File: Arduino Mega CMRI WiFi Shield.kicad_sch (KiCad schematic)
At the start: 22 parts, among them J10 61300411121, J11 61300411121, J12 61300411121, J13 61300411121, J14 61300411121, J15 61300411121, J16 61300411121, J17 61300411121, J18 61300311121, J2 61300411121, J3 61300411121, J4 61300411121, J5 61300411121, J6 61300411121, J7 61300411121, J8 61300411121, J9 61300411121

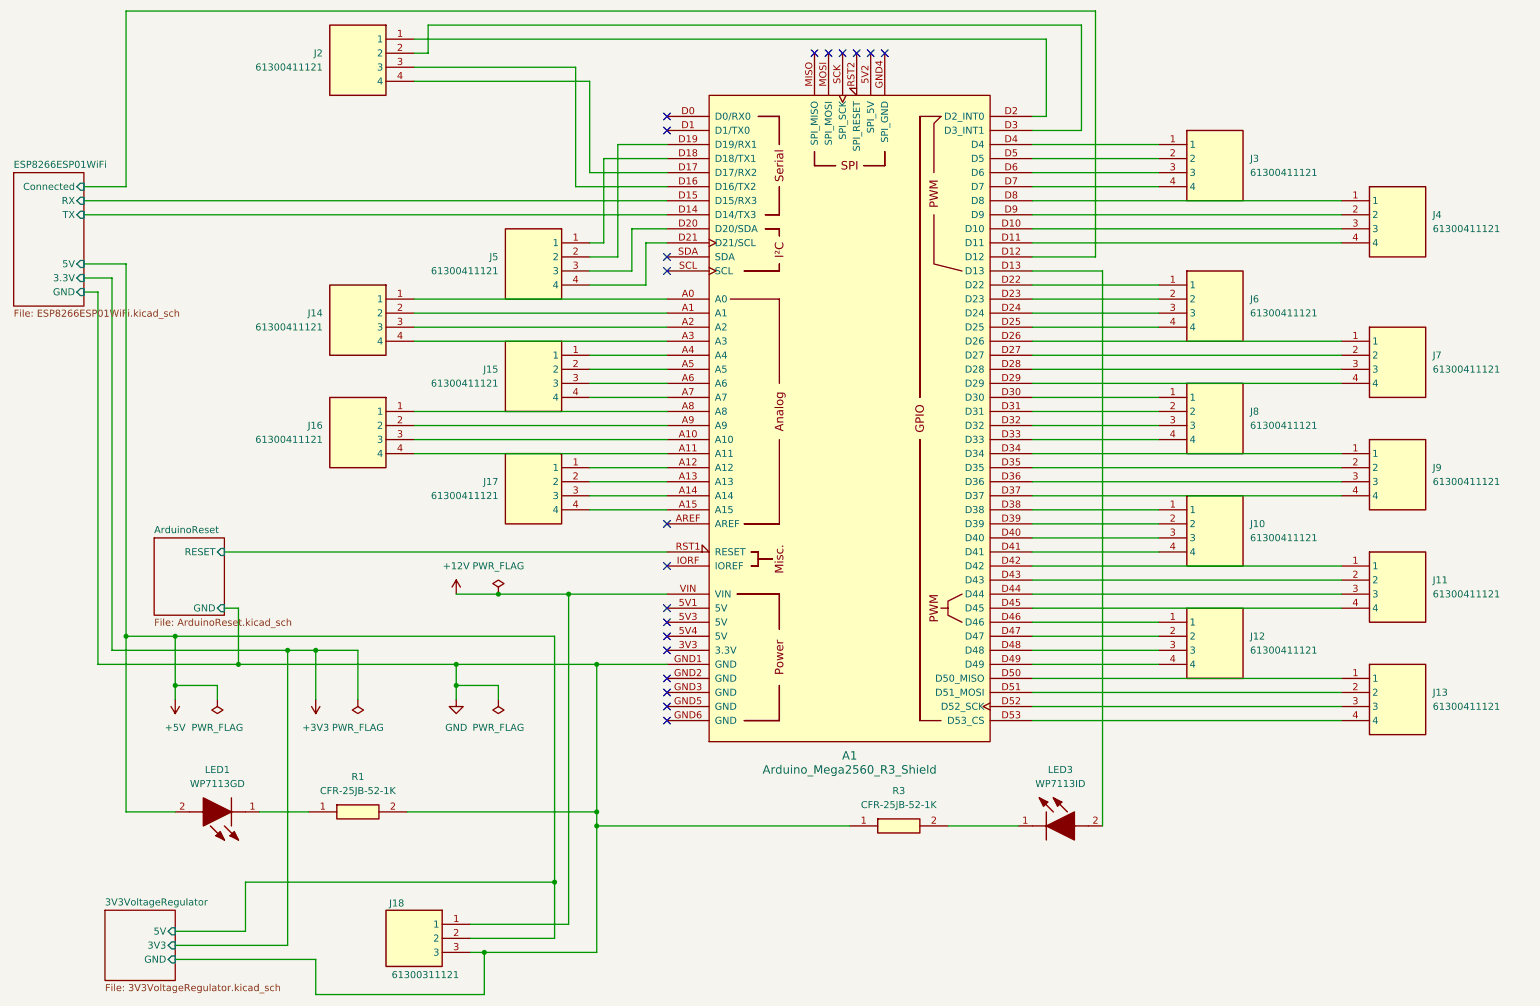
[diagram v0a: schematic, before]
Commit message: Swapped components for those in custom library, updated labelling on PCB.
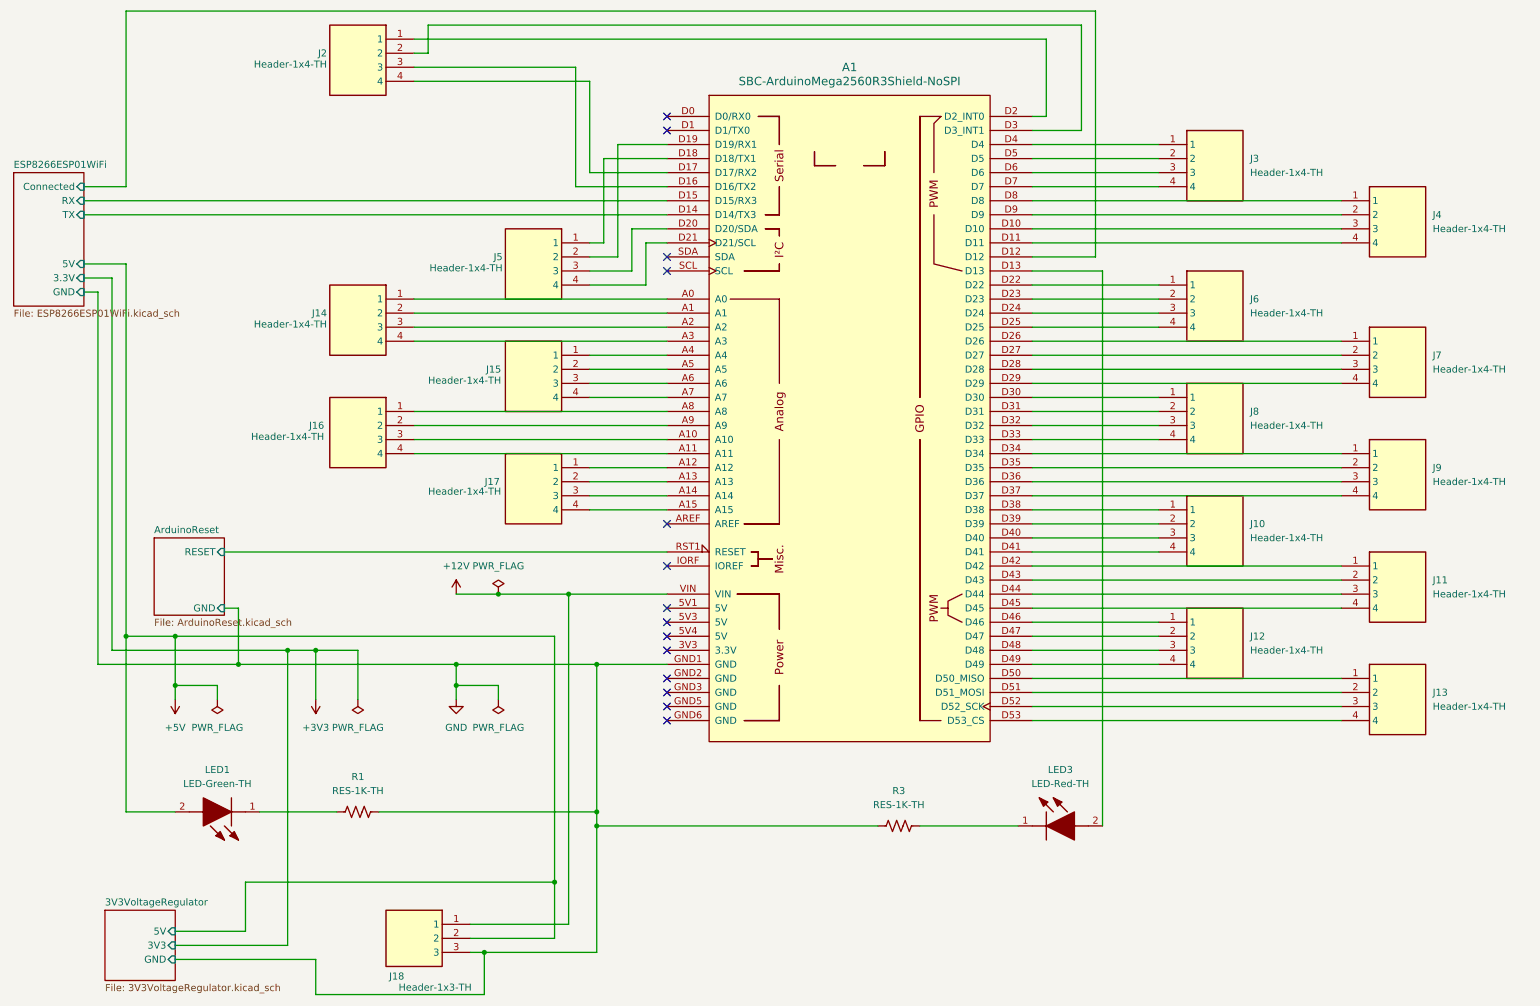
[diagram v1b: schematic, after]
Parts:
- A1: value Arduino_Mega2560_R3_Shield -> SBC-ArduinoMega2560R3Shield-NoSPI; footprint PCM_arduino-library:Arduino_Mega2560_R3_Shield -> Custom:SBC-ArduinoMega2560R3Shield-NoSPI; symbol PCM_arduino-library:Arduino_Mega2560_R3_Shield -> Custom:SBC-ArduinoMega2560R3Shield-NoSPI
- J10, J11, J12, J13, J14, J15, J16, J17, J2, J3, J4, J5, J6, J7, J8, J9: value 61300411121 -> Header-1x4-TH; footprint SamacSys_Parts:HDRV4W95P0X254_1X4_1016X254X854P -> Custom:710-61300411121; symbol SamacSys_Parts:61300411121 -> Custom:Header-1x4-TH; Supplier (none) -> Mouser; Supplier Part Number (none) -> 710-61300411121; Supplier Price/Stock (none) -> https://www.mouser.co.uk/ProductDetail/Wurth-Elektronik/613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
- J18: value 61300311121 -> Header-1x3-TH; footprint SamacSys_Parts:HDRV3W64P0X254_1X3_762X254X869P -> Custom:710-61300311121; symbol SamacSys_Parts:61300311121 -> Custom:Header-1x3-TH; Supplier (none) -> Mouser; Supplier Part Number (none) -> 710-61300311121; Supplier Price/Stock (none) -> https://www.mouser.co.uk/ProductDetail/Wurth-Elektronik/613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
- LED1: value WP7113GD -> LED-Green-TH; footprint SamacSys_Parts:L53ND -> Custom:604-WP7113GD; symbol SamacSys_Parts:WP7113GD -> Custom:LED-Green-TH; Supplier (none) -> Mouser; Supplier Part Number (none) -> 604-WP7113GD; Supplier Price/Stock (none) -> https://www.mouser.co.uk/ProductDetail/Kingbright/WP7113GD?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
- LED3: value WP7113ID -> LED-Red-TH; footprint SamacSys_Parts:L53ND -> Custom:604-WP7113ID; symbol SamacSys_Parts:WP7113ID -> Custom:LED-Red-TH; Supplier (none) -> Mouser; Supplier Part Number (none) -> 604-WP7113ID; Supplier Price/Stock (none) -> https://www.mouser.co.uk/ProductDetail/Kingbright/WP7113ID?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
- R1, R3: value CFR-25JB-52-1K -> RES-1K-TH; footprint SamacSys_Parts:RESAD1590W60L630D240 -> Resistor_THT:R_Axial_DIN0204_L3.6mm_D1.6mm_P7.62mm_Horizontal; symbol SamacSys_Parts:CFR-25JB-52-1K -> Custom:Res-1K-TH; Manufacturer_Name KEMET -> YAGEO; Manufacturer_Part_Number CFR-25JB-52-1K -> CFR-25JR-52-1K; Supplier (none) -> Mouser; Supplier Part Number (none) -> 603-CFR-25JR-521K; Supplier Price/Stock (none) -> https://www.mouser.com/ProductDetail/YAGEO/CFR-25JR-52-1K?q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
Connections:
- no-connect marks 20 -> 14

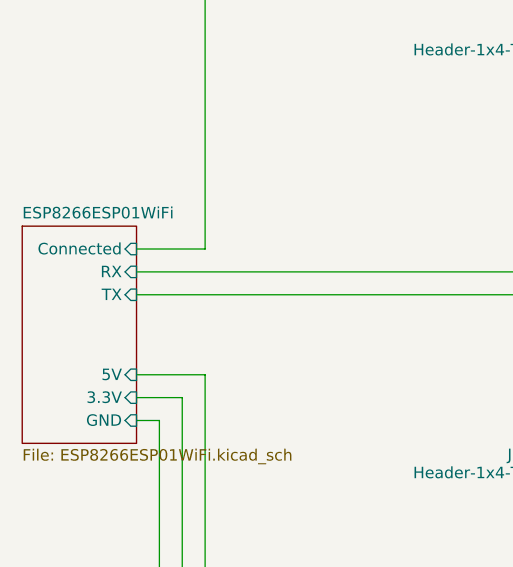
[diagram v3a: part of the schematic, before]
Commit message: Swapped the RX and TX pins between the arduino and the ESP8266-ESP01 that was discovered on prototype board v1.2
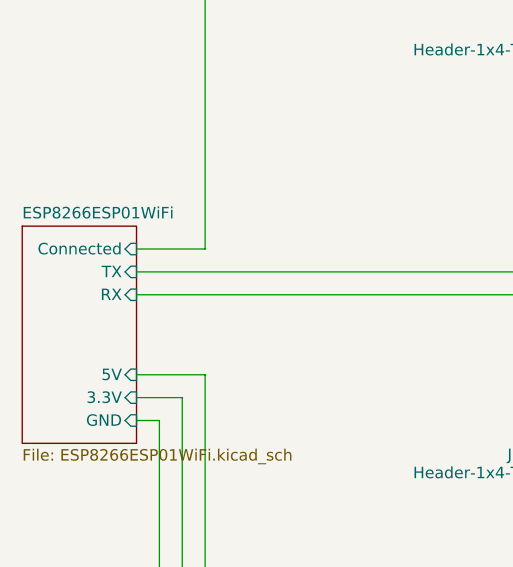
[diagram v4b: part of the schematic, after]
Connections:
- net ESP8266ESP01WiFi/RX: now also A1.D14 (D14/TX3); no longer A1.D15 (D15/RX3)
- net ESP8266ESP01WiFi/TX: now also A1.D15 (D15/RX3); no longer A1.D14 (D14/TX3)
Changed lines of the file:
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@@
 	(wire
 		(pts
-			(xy 34.29 52.07) (xy 139.7 52.07)
+			(xy 34.29 49.53) (xy 139.7 49.53)
 		)
 		(stroke
@@
 	(wire
 		(pts
-			(xy 34.29 49.53) (xy 139.7 49.53)
+			(xy 34.29 52.07) (xy 139.7 52.07)
 		)
 		(stroke
@@
 		)
 		(pin "RX" input
-			(at 34.29 49.53 0)
+			(at 34.29 52.07 0)
 			(effects
 				(font
@@
 		)
 		(pin "TX" input
-			(at 34.29 52.07 0)
+			(at 34.29 49.53 0)
 			(effects
 				(font
